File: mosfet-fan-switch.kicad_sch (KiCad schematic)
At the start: 16 parts, among them Q1 irfz44n, Q2 2n7002, Q3 irf7416, U1 Arduino_Pro_Mini_3V3

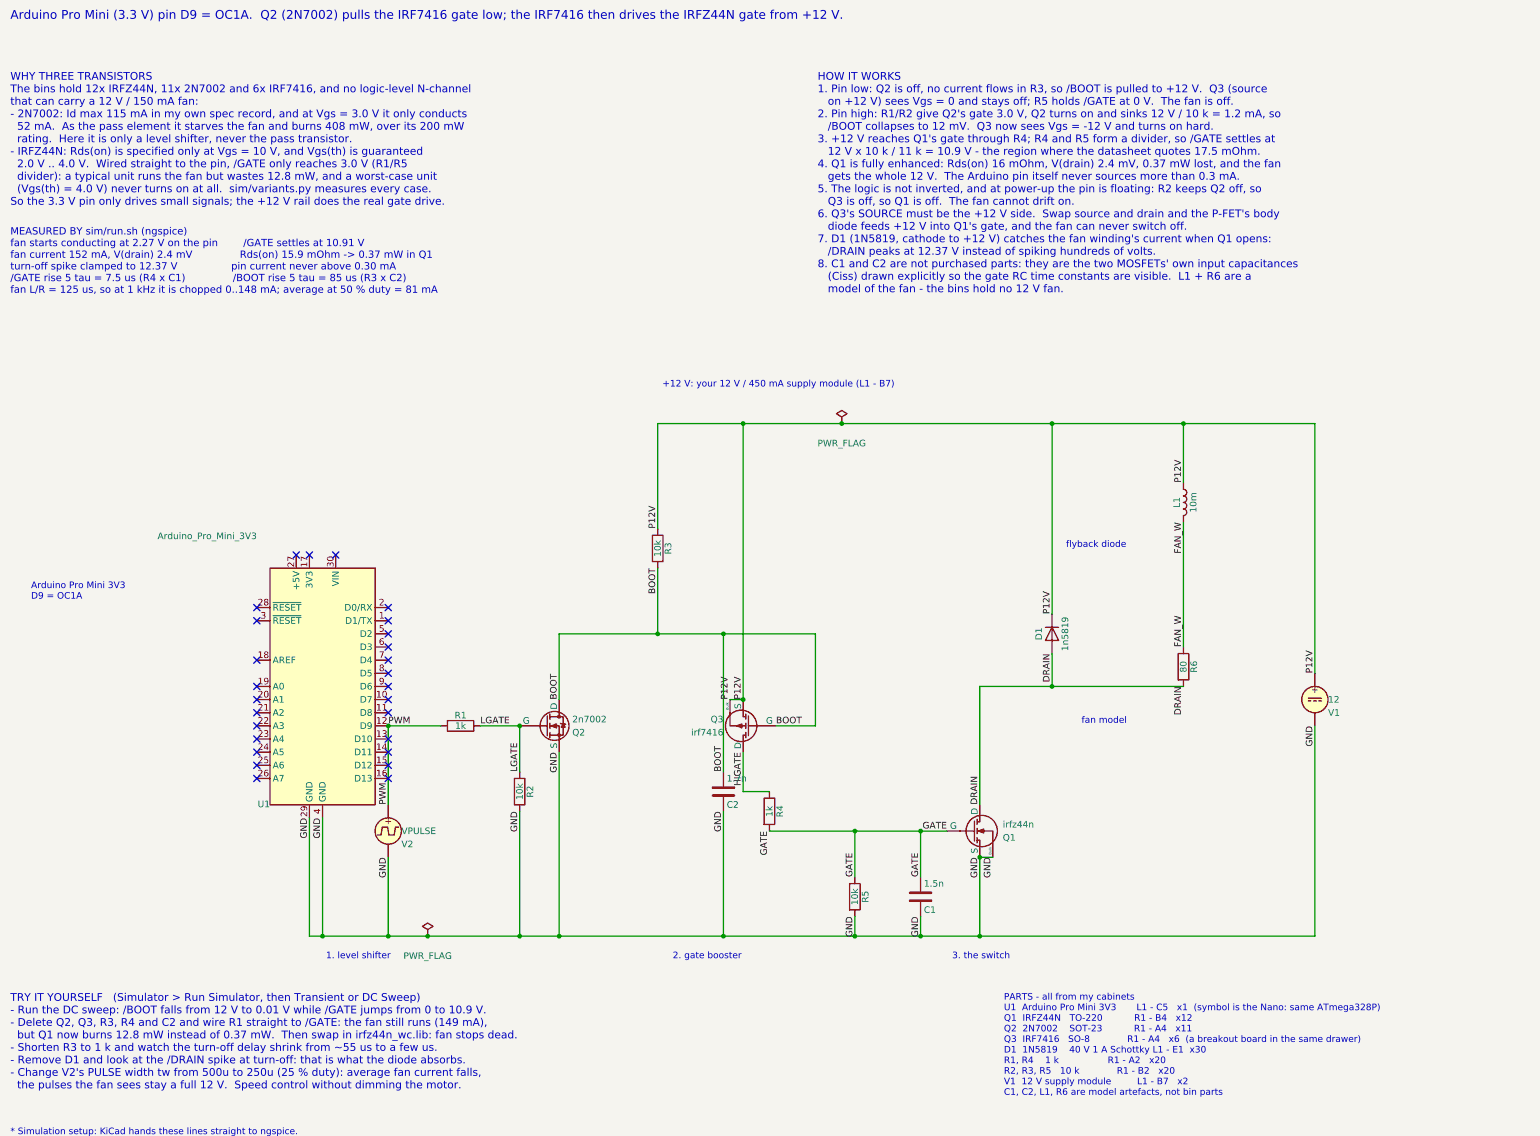
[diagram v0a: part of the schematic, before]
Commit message: Size the fan model to my real fans (100 mA) and check 1-4 fans on one output
R6 on the sheet is now 120 ohm, so the fan model (10 mH + 120 ohm) draws the
100 mA my actual 12 V fans draw instead of 150 mA.  Every quoted number in the
sheet text, the README and the plots follows: fan 102 mA, V(drain) 1.6 mV,
Rds 15.7 mOhm, 0.16 mW in Q1, spike clamped at 12.36 V, fan L/R 83 us, average
54 mA at 1 kHz / 50 %.

New sim/fan_count.py clones the sheet's fan branch 1..4 times (it reads L and R
from the exported netlist so the sheet stays the source of truth) and checks the
result against the ratings of the parts that actually carry load current:

  3 fans: 302 mA total, 4.8 mV at the drain, 1.46 mW in Q1,
          295 mA peaks through the 1N5819 (1 A part), 141 mA average from the
          12 V / 450 mA module  ->  fits, with room
  4 fans: 402 mA total, 392 mA peak through D1 -> still fits, but the supply is
          then nearly fully loaded; three 150 mA fans would not fit at all.

Gate drive is unchanged by the load, so the booster's parts are unaffected.
plotted in sim/out/fan_count.png, table in sim/out/fan_count.csv, and run.sh now
runs it as the last step.
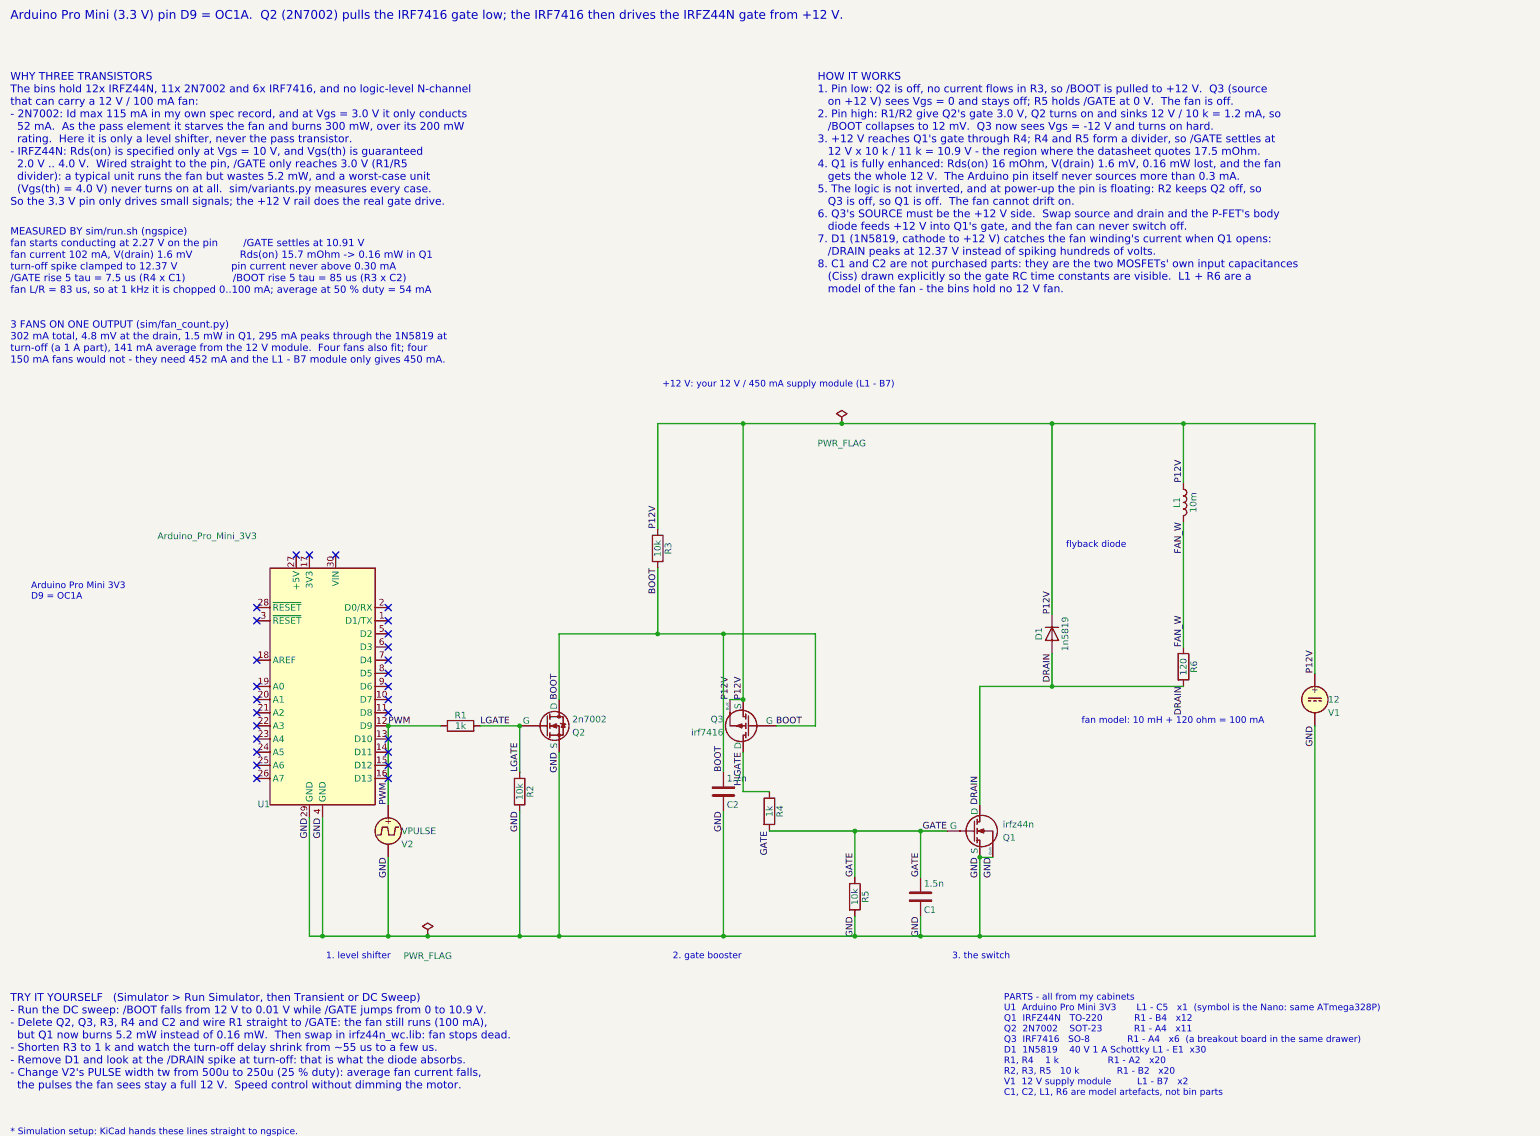
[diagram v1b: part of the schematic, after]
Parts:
- R6: value 80 -> 120
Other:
- note added: "3 FANS ON ONE OUTPUT (sim/fan_count.py) 302 mA total, 4.8 mV at the drain, 1.5 mW in Q1, 295 mA peaks through the 1N5819 at turn-off (a 1 A part), 141 mA average from the 12 V module. Four fans also fit; four 150 mA fans would not - they need 452 mA and the L1 - B7 module only gives 450 mA."
- note added: "MEASURED BY sim/run.sh (ngspice) fan starts conducting at 2.27 V on the pin /GATE settles at 10.91 V fan current 102 mA, V(drain) 1.6 mV Rds(on) 15.7 mOhm -> 0.16 mW in Q1 turn-off spike clamped to 12.37 V pin current never above 0.30 mA /GATE rise 5 tau = 7.5 us (R4 x C1) /BOOT rise 5 tau = 85 us (R3 x C2) fan L/R = 83 us, so at 1 kHz it is chopped 0..100 mA; average at 50 % duty = 54 mA"
- note added: "TRY IT YOURSELF (Simulator > Run Simulator, then Transient or DC Sweep) - Run the DC sweep: /BOOT falls from 12 V to 0.01 V while /GATE jumps from 0 to 10.9 V. - Delete Q2, Q3, R3, R4 and C2 and wire R1 straight to /GATE: the fan still runs (100 mA), but Q1 now burns 5.2 mW instead of 0.16 mW. Then swap in irfz44n_wc.lib: fan stops dead. - Shorten R3 to 1 k and watch the turn-off delay shrink fro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"
- note added: "WHY THREE TRANSISTORS The bins hold 12x IRFZ44N, 11x 2N7002 and 6x IRF7416, and no logic-level N-channel that can carry a 12 V / 100 mA fan: - 2N7002: Id max 115 mA in my own spec record, and at Vgs = 3.0 V it only conducts 52 mA. As the pass element it starves the fan and burns 300 mW, over its 200 mW rating. Here it is only a level shifter, never the pass transistor. - IRFZ44N: Rds(on) is speci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"
- note added: "fan model: 10 mH + 120 ohm = 100 mA"
- note removed: "MEASURED BY sim/run.sh (ngspice) fan starts conducting at 2.27 V on the pin /GATE settles at 10.91 V fan current 152 mA, V(drain) 2.4 mV Rds(on) 15.9 mOhm -> 0.37 mW in Q1 turn-off spike clamped to 12.37 V pin current never above 0.30 mA /GATE rise 5 tau = 7.5 us (R4 x C1) /BOOT rise 5 tau = 85 us (R3 x C2) fan L/R = 125 us, so at 1 kHz it is chopped 0..148 mA; average at 50 % duty = 81 mA"
- note removed: "TRY IT YOURSELF (Simulator > Run Simulator, then Transient or DC Sweep) - Run the DC sweep: /BOOT falls from 12 V to 0.01 V while /GATE jumps from 0 to 10.9 V. - Delete Q2, Q3, R3, R4 and C2 and wire R1 straight to /GATE: the fan still runs (149 mA), but Q1 now burns 12.8 mW instead of 0.37 mW. Then swap in irfz44n_wc.lib: fan stops dead. - Shorten R3 to 1 k and watch the turn-off delay shrink fr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"
- note removed: "WHY THREE TRANSISTORS The bins hold 12x IRFZ44N, 11x 2N7002 and 6x IRF7416, and no logic-level N-channel that can carry a 12 V / 150 mA fan: - 2N7002: Id max 115 mA in my own spec record, and at Vgs = 3.0 V it only conducts 52 mA. As the pass element it starves the fan and burns 408 mW, over its 200 mW rating. Here it is only a level shifter, never the pass transistor. - IRFZ44N: Rds(on) is speci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"
- note removed: "fan model"
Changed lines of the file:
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@@
 			)
 		)
-		(property "Value" "80"
+		(property "Value" "120"
 			(at 266.7 158.75 90)
 			(show_name no)
@@
 		)
 	)
-	(text "WHY THREE TRANSISTORS\nThe bins hold 12x IRFZ44N, 11x 2N7002 and 6x IRF7416, and no logic-level N-channel\nthat can carry a 12 V / 150 mA fan:\n- 2N7002: Id max 115 mA in my own spec record, and at Vgs = 3.0 V it only conducts\n  52 mA.  As the pass element it starves the fan and burns 408 mW, over its 200 mW\n  rating.  Here it is only a level shifter, never the pass transistor.\n- IRFZ44N: Rds(on) is specified only at Vgs = 10 V, and Vgs(th) is guaranteed\n  2.0 V .. 4.0 V.  Wired straight to the pin, /GATE only reaches 3.0 V (R1/R5\n  divider): a typical unit runs the fan but wastes 12.8 mW, and a worst-case unit\n  (Vgs(th) = 4.0 V) never turns on at all.  sim/variants.py measures every case.\nSo the 3.3 V pin only drives small signals; the +12 V rail does the real gate drive."
+	(text "WHY THREE TRANSISTORS\nThe bins hold 12x IRFZ44N, 11x 2N7002 and 6x IRF7416, and no logic-level N-channel\nthat can carry a 12 V / 100 mA fan:\n- 2N7002: Id max 115 mA in my own spec record, and at Vgs = 3.0 V it only conducts\n  52 mA.  As the pass element it starves the fan and burns 300 mW, over its 200 mW\n  rating.  Here it is only a level shifter, never the pass transistor.\n- IRFZ44N: Rds(on) is specified only at Vgs = 10 V, and Vgs(th) is guaranteed\n  2.0 V .. 4.0 V.  Wired straight to the pin, /GATE only reaches 3.0 V (R1/R5\n  divider): a typical unit runs the fan but wastes 5.2 mW, and a worst-case unit\n  (Vgs(th) = 4.0 V) never turns on at all.  sim/variants.py measures every case.\nSo the 3.3 V pin only drives small signals; the +12 V rail does the real gate drive."
 		(exclude_from_sim no)
 		(at 40 44 0)
@@
 		)
 	)
-	(text "HOW IT WORKS\n1. Pin low: Q2 is off, no current flows in R3, so /BOOT is pulled to +12 V.  Q3 (source\n   on +12 V) sees Vgs = 0 and stays off; R5 holds /GATE at 0 V.  The fan is off.\n2. Pin high: R1/R2 give Q2's gate 3.0 V, Q2 turns on and sinks 12 V / 10 k = 1.2 mA, so\n   /BOOT collapses to 12 mV.  Q3 now sees Vgs = -12 V and turns on hard.\n3. +12 V reaches Q1's gate through R4; R4 and R5 form a divider, so /GATE settles at\n   12 V x 10 k / 11 k = 10.9 V - the region where the datasheet quotes 17.5 mOhm.\n4. Q1 is fully enhanced: Rds(on) 16 mOhm, V(drain) 2.4 mV, 0.37 mW lost, and the fan\n   gets the whole 12 V.  The Arduino pin itself never sources more than 0.3 mA.\n5. The logic is not inverted, and at power-up the pin is floating: R2 keeps Q2 off, so\n   Q3 is off, so Q1 is off.  The fan cannot drift on.\n6. Q3's SOURCE must be the +12 V side.  Swap source and drain and the P-FET's body\n   diode feeds +12 V into Q1's gate, and the fan can never switch off.\n7. D1 (1N5819, cathode to +12 V) catches the fan winding's current when Q1 opens:\n   /DRAIN peaks at 12.37 V instead of spiking hundreds of volts.\n8. C1 and C2 are not purchased parts: they are the two MOSFETs' own input capacitances\n   (Ciss) drawn explicitly so the gate RC time constants are visible.  L1 + R6 are a\n   model of the fan - the bins hold no 12 V fan."
+	(text "HOW IT WORKS\n1. Pin low: Q2 is off, no current flows in R3, so /BOOT is pulled to +12 V.  Q3 (source\n   on +12 V) sees Vgs = 0 and stays off; R5 holds /GATE at 0 V.  The fan is off.\n2. Pin high: R1/R2 give Q2's gate 3.0 V, Q2 turns on and sinks 12 V / 10 k = 1.2 mA, so\n   /BOOT collapses to 12 mV.  Q3 now sees Vgs = -12 V and turns on hard.\n3. +12 V reaches Q1's gate through R4; R4 and R5 form a divider, so /GATE settles at\n   12 V x 10 k / 11 k = 10.9 V - the region where the datasheet quotes 17.5 mOhm.\n4. Q1 is fully enhanced: Rds(on) 16 mOhm, V(drain) 1.6 mV, 0.16 mW lost, and the fan\n   gets the whole 12 V.  The Arduino pin itself never sources more than 0.3 mA.\n5. The logic is not inverted, and at power-up the pin is floating: R2 keeps Q2 off, so\n   Q3 is off, so Q1 is off.  The fan cannot drift on.\n6. Q3's SOURCE must be the +12 V side.  Swap source and drain and the P-FET's body\n   diode feeds +12 V into Q1's gate, and the fan can never switch off.\n7. D1 (1N5819, cathode to +12 V) catches the fan winding's current when Q1 opens:\n   /DRAIN peaks at 12.37 V instead of spiking hundreds of volts.\n8. C1 and C2 are not purchased parts: they are the two MOSFETs' own input capacitances\n   (Ciss) drawn explicitly so the gate RC time constants are visible.  L1 + R6 are a\n   model of the fan - the bins hold no 12 V fan."
 		(exclude_from_sim no)
 		(at 196 44 0)
@@
 		)
 	)
-	(text "MEASURED BY sim/run.sh (ngspice)\nfan starts conducting at 2.27 V on the pin        /GATE settles at 10.91 V\nfan current 152 mA, V(drain) 2.4 mV               Rds(on) 15.9 mOhm -> 0.37 mW in Q1\nturn-off spike clamped to 12.37 V                 pin current never above 0.30 mA\n/GATE rise 5 tau = 7.5 us (R4 x C1)               /BOOT rise 5 tau = 85 us (R3 x C2)\nfan L/R = 125 us, so at 1 kHz it is chopped 0..148 mA; average at 50 % duty = 81 mA"
+	(text "MEASURED BY sim/run.sh (ngspice)\nfan starts conducting at 2.27 V on the pin        /GATE settles at 10.91 V\nfan current 102 mA, V(drain) 1.6 mV               Rds(on) 15.7 mOhm -> 0.16 mW in Q1\nturn-off spike clamped to 12.37 V                 pin current never above 0.30 mA\n/GATE rise 5 tau = 7.5 us (R4 x C1)               /BOOT rise 5 tau = 85 us (R3 x C2)\nfan L/R = 83 us, so at 1 kHz it is chopped 0..100 mA; average at 50 % duty = 54 mA"
 		(exclude_from_sim no)
 		(at 40 74 0)
@@
 		)
 	)
-	(text "TRY IT YOURSELF   (Simulator > Run Simulator, then Transient or DC Sweep)\n- Run the DC sweep: /BOOT falls from 12 V to 0.01 V while /GATE jumps from 0 to 10.9 V.\n- Delete Q2, Q3, R3, R4 and C2 and wire R1 straight to /GATE: the fan still runs (149 mA),\n  but Q1 now burns 12.8 mW instead of 0.37 mW.  Then swap in irfz44n_wc.lib: fan stops dead.\n- Shorten R3 to 1 k and watch the turn-off delay shrink from ~55 us to a few us.\n- Remove D1 and look at the /DRAIN spike at turn-off: that is what the diode absorbs.\n- Change V2's PULSE width tw from 500u to 250u (25 % duty): average fan current falls,\n  the pulses the fan sees stay a full 12 V.  Speed control without dimming the motor."
+	(text "TRY IT YOURSELF   (Simulator > Run Simulator, then Transient or DC Sweep)\n- Run the DC sweep: /BOOT falls from 12 V to 0.01 V while /GATE jumps from 0 to 10.9 V.\n- Delete Q2, Q3, R3, R4 and C2 and wire R1 straight to /GATE: the fan still runs (100 mA),\n  but Q1 now burns 5.2 mW instead of 0.16 mW.  Then swap in irfz44n_wc.lib: fan stops dead.\n- Shorten R3 to 1 k and watch the turn-off delay shrink from ~55 us to a few us.\n- Remove D1 and look at the /DRAIN spike at turn-off: that is what the diode absorbs.\n- Change V2's PULSE width tw from 500u to 250u (25 % duty): average fan current falls,\n  the pulses the fan sees stay a full 12 V.  Speed control without dimming the motor."
 		(exclude_from_sim no)
 		(at 40 222 0)
@@
 		)
 	)
-	(text "fan model"
+	(text "fan model: 10 mH + 120 ohm = 100 mA"
 		(exclude_from_sim no)
 		(at 247 170 0)
@@
 		)
 	)
+	(text "3 FANS ON ONE OUTPUT (sim/fan_count.py)\n302 mA total, 4.8 mV at the drain, 1.5 mW in Q1, 295 mA peaks through the 1N5819 at\nturn-off (a 1 A part), 141 mA average from the 12 V module.  Four fans also fit; four\n150 mA fans would not - they need 452 mA and the L1 - B7 module only gives 450 mA."
+		(exclude_from_sim no)
+		(at 40 92 0)
+		(effects
+			(font
+				(size 1.4 1.4)
+			)
+			(justify left top)
+		)
+	)

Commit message: Single-layer PCB for the fan driver: 56 x 44 mm, all copper on B.Cu, DRC clean
pcb/build_board.py generates the board from a part table, a track list and the
design rules, embedding the KiCad library footprints it needs. Re-running it is
a no-op: ids are derived from the content (uuid5) and the 14 electrical footprints
reuse their symbols' uuids from the sheet, so cross-probing and Update PCB from
Schematic treat the board as the same 14 parts instead of 18 unknown ones.

Home-etch rules in the .kicad_pro netclass (clearance 0.50 mm, min track 0.80 mm)
instead of KiCad's fab defaults. Result:

  Found 0 violations
  Found 0 unconnected items

56 x 44 mm (the four 3.2 mm M3 holes set the size), 18 footprints, 42 segments,
zero vias: Q2 (SOT-23) and Q3 (SO-8) sit on the copper side, which is what removes
the need for a via anywhere. /GND bus 2.0 mm along the top edge, /P12V bus 3.0 mm
along the bottom, a 1.5 mm GND return lane down the left edge, 1.5 mm /DRAIN runs.
The generator checks every net pair for crossings: no net crossings, so the 0 ohm
jumper trick was never needed.

Schematic: J1/J2/J3 connectors with (exclude_from_sim yes) - without it KiCad
exported "J1 __J1" and ngspice reads a leading J as a JFET; C3 100n and C4 10u
decoupling at the 12 V input (sim-neutral: every number in sim/run.sh is
unchanged); footprints corrected to the real packages; DNP on the model artefacts
C1, C2, L1, R6, U1, V1, V2; and a PHYSICAL PINOUTS note block, because the SPICE
symbols number MOSFET pins D-G-S while SOT-23 is 1 gate / 2 source / 3 drain, the
IRF7416 SO-8 is 1-3 source / 4 gate / 5-8 drain and the IRFZ44N TO-220 is
1 gate / 2 drain / 3 source. ERC: 0 errors, 0 warnings.

KiCad 10 behaviour that had to be pinned down before the DRC would go clean:

- A footprint's placement rotation rotates pad *positions* only; a pad's copper
  rotates only by that pad's own (at x y angle). KiCad bakes the angle into every
  pad when it places a footprint (a fresh SO-8 at (at 10 10 9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
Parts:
- added C3: 100n, Capacitor_THT:C_Disc_D5.0mm_W2.5mm_P5.00mm, symbol Device:C
- added C4: 10u, Capacitor_THT:CP_Radial_D6.3mm_P2.50mm, symbol Device:C
- added J1: 12V IN, Connector_PinHeader_2.54mm:PinHeader_1x02_P2.54mm_Vertical, symbol Connector:Conn_01x02_Pin
- added J2: PWM IN, Connector_PinHeader_2.54mm:PinHeader_1x02_P2.54mm_Vertical, symbol Connector:Conn_01x02_Pin
- added J3: FAN OUT, Connector_PinHeader_2.54mm:PinHeader_2x03_P2.54mm_Vertical, symbol Connector_Generic:Conn_02x03_Counter_Clockwise
- C1, C2, V1, V2: now not fitted
- L1: footprint Inductor_THT:L_Axial_L9.5mm_D4.0mm_P12.70mm_Horizontal_Fastron_SMCC -> (none); now not fitted
- Q3: footprint Package_SO:PowerPAK_SO-8_Single -> Package_SO:SO-8_3.9x4.9mm_P1.27mm
- R1, R2, R3, R4, R5: footprint Resistor_THT:R_Axial_DIN0207_L6.3mm_D2.5mm_P10.16mm_Horizontal -> Resistor_THT:R_Axial_DIN0207_L6.3mm_D2.5mm_P7.62mm_Horizontal
- R6: footprint Resistor_THT:R_Axial_DIN0207_L6.3mm_D2.5mm_P10.16mm_Horizontal -> (none); now not fitted
- U1: footprint Module:Arduino_Nano -> (none); now not fitted
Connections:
- net DRAIN: now also J3.2 (Pin_2), J3.4 (Pin_4), J3.6 (Pin_6)
- net GND: now also C3.2, C4.2, J1.2 (Pin_2), J2.2 (Pin_2)
- net P12V: now also C3.1, C4.1, J1.1 (Pin_1), J3.1 (Pin_1), J3.3 (Pin_3), J3.5 (Pin_5)
- net PWM: now also J2.1 (Pin_1)
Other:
- note added: "PHYSICAL PINOUTS - the board follows the package, not the symbol's pin order Q2 2N7002 SOT-23 1 gate /LGATE 2 source /GND 3 drain /BOOT Q3 IRF7416 SO-8 1,2,3 source /P12V 4 gate /BOOT 5..8 drain /HIGATE Q1 IRFZ44N TO-220 1 gate /GATE 2 drain /DRAIN 3 source /GND D1 1N5819 DO-41 banded end (cathode) to +12 V, other end to /DRAIN J3 3 fans odd pins = +12 V, even pins = the switched /DRAIN side The 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"
